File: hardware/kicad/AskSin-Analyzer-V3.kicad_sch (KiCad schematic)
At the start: 32 parts, among them J1 Pi GPIO, J2 AVR-ISP-6, J5 OLED I2C, J6 Taster, J7 WS2812, U1 MCP1754S-3302xCB, U2 ATmega328P-AU, U3 E07-900M10S, Y1 8MHz

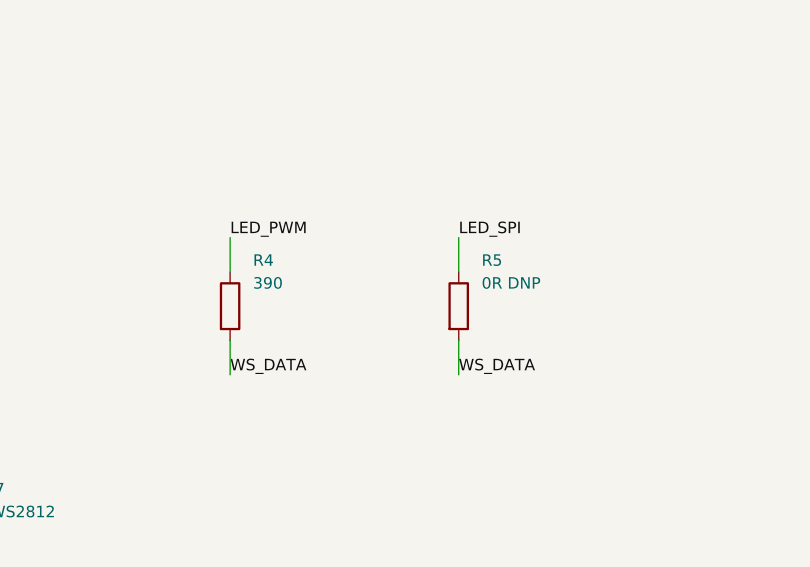
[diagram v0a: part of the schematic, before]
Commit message: Fertigungsdaten: R5 statt R4 bestückt, S1 → C231329, Y1 → C83707
Die Bestückungsvorgabe der WS2812-Datenleitung wechselt auf die
SPI-Brücke R5 (0 Ω, GPIO10, JLCPCB C17477 Basic) — den Weg nutzt die
Analyzer-Software. R4 (390 Ω, PWM/GPIO18) bleibt als dokumentierte,
unbestückte Alternative. Nur Bestückungsdaten und Werte-Texte geändert,
die Platine (Routing, Produktionsstand) ist unberührt.

Außerdem in der JLCPCB-Bestückung:
- S1 → C231329 (B3U-1000P ohne Zentrierstift; gleiche Pads, die
  Stiftbohrung bleibt leer) — C231330 war nicht lieferbar
- Y1 → C83707 (Murata CSTLS8M00G53-B0, THT-Ausnahme, Wellenlöten);
  von Hand bleiben nur noch Funkmodul und Steckverbinder

Nachgezogen: bom/cpl/jlcpcb-Dateien, Stückliste, Schaltplan-PDF
(nur Werte-Texte, ERC weiter 0/0), Fertigungs-Zip samt LIESMICH,
Reichelt-Bestellliste, Hardware-README, Status-LED-Doku, Handbuch.
generate_schematic.py überschreibt eine vorhandene .kicad_pro nicht
mehr (dort stecken die Board-Designregeln).

Co-Authored-By: Claude Fable 5 <noreply@anthropic.com>
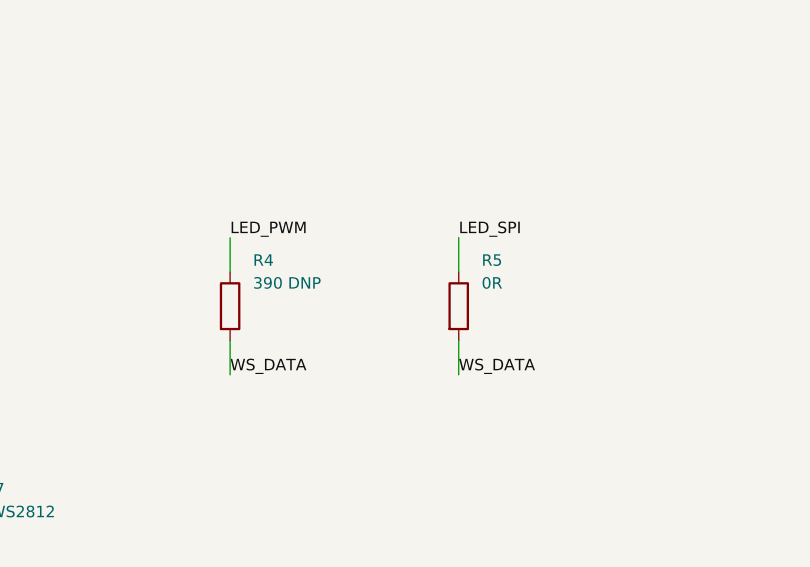
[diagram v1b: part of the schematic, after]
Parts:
- R4: value 390 -> 390 DNP
- R5: value 0R DNP -> 0R
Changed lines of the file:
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@@
 			(effects (font (size 1.27 1.27)) (justify left))
 		)
-		(property "Value" "390"
+		(property "Value" "390 DNP"
 			(at 121.92 237.49 0)
 			(effects (font (size 1.27 1.27)) (justify left))
@@
 			(effects (font (size 1.27 1.27)) (justify left))
 		)
-		(property "Value" "0R DNP"
+		(property "Value" "0R"
 			(at 147.32 237.49 0)
 			(effects (font (size 1.27 1.27)) (justify left))

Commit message: Status-LED D1 entpolt — sie konnte nie leuchten
Im KiCad-Symbol Device:LED ist Pin 1 die Kathode. Auf der Platine lag
Pin 1 an R1 (also am Treiber) und Pin 2, die Anode, an Masse. Die
Firmware schaltet ihren Pin aktiv auf HIGH (AskSinPP Led::ledOn ->
setHigh, invert() wird nie gesetzt), der Strom hätte also von Masse
gegen die Diodenrichtung zum Mikrocontroller fließen müssen.

Netzliste korrigiert: LED_TREIBER (U2.2 -> R1.1), LED_ANODE
(R1.2 -> D1.2), D1.1 an GND. Nachgerechnet: 3,9 mA bei 3,3 V und
330 Ohm mit einer roten LED — passt zu R1.

Bei der Gelegenheit ein Loch in der eigenen Prüfkette geschlossen:
rebuild.py verglich gegen die zuletzt abgelegte netlist.net statt gegen
einen frischen Export. Nach einer Schaltplanänderung prüfte es damit
gegen einen veralteten Stand — genau die Sorte stiller Fehler, die man
nicht bemerkt. Der Export läuft jetzt vor jeder Prüfung.

ERC 0/0, DRC 0/0, Netzliste exakt, alle Massepads angebunden.
Fertigungspaket und Handbuchbilder neu erzeugt.

Co-Authored-By: Claude Fable 5 <noreply@anthropic.com>
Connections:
- net GND: now also D1.1 (K); no longer D1.2 (A)
- net LED_A renamed LED_TREIBER
- net LED_K renamed LED_ANODE
- net LED_ANODE: now also D1.2 (A); no longer D1.1 (K)
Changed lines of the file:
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@@
 		(effects (font (size 1.27 1.27)) (justify left bottom))
 	)
-	(wire (pts (xy 316.23 190.5) (xy 320.04 190.5))
+	(wire (pts (xy 308.61 190.5) (xy 304.8 190.5))
 		(stroke (width 0) (type default))
 	)
 	(label "GND"
-		(at 320.04 190.5 0)
+		(at 304.8 190.5 0)
 		(fields_autoplaced yes)
 		(effects (font (size 1.27 1.27)) (justify left bottom))
@@
 		(stroke (width 0) (type default))
 	)
-	(label "LED_A"
+	(label "LED_TREIBER"
 		(at 269.24 152.4 0)
 		(fields_autoplaced yes)
@@
 		(stroke (width 0) (type default))
 	)
-	(label "LED_A"
+	(label "LED_TREIBER"
 		(at 292.1 182.88 0)
 		(fields_autoplaced yes)
@@
 		(stroke (width 0) (type default))
 	)
-	(label "LED_K"
+	(label "LED_ANODE"
 		(at 292.1 198.12 0)
 		(fields_autoplaced yes)
 		(effects (font (size 1.27 1.27)) (justify left bottom))
 	)
-	(wire (pts (xy 308.61 190.5) (xy 304.8 190.5))
-		(stroke (width 0) (type default))
-	)
-	(label "LED_K"
-		(at 304.8 190.5 0)
-		(fields_autoplaced yes)
-		(effects (font (size 1.27 1.27)) (justify left bottom))
+	(wire (pts (xy 316.23 190.5) (xy 320.04 190.5))
+		(stroke (width 0) (type default))
+	)
+	(label "LED_ANODE"
+		(at 320.04 190.5 0)
+		(fields_autoplaced yes)
+		(effects (font (size 1.27 1.27)) (justify left bottom))

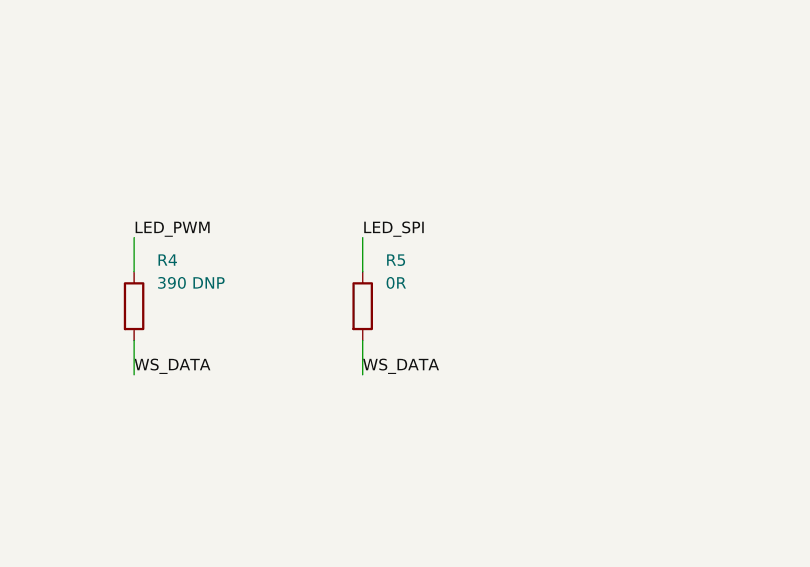
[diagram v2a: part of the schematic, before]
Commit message: R5 von 0 Ohm auf 330 Ohm — der Serienwiderstand des Vorbilds fehlte
Das Status-LED-OLED-Projekt fuehrt die WS2812-Datenleitung fuer *beide*
Ansteuerarten ueber 330-470 Ohm. Auf dem SPI-Weg war R5 bei uns eine
0-Ohm-Bruecke, der Widerstand fehlte dort also ganz. Jetzt 330 Ohm —
dasselbe Bauteil wie R1 (JLCPCB C17630), damit faellt sogar eine
Position in der Stueckliste weg (10 statt 11).

Signaltechnisch geprueft: 330 Ohm an der Eingangskapazitaet der LED
ergibt rund 5 ns Anstiegszeit gegen 420 ns kuerzeste Pulsdauer bei
2,4 MHz — unkritisch.

DRC 0/0, Netzliste exakt, alle Massepads angebunden.

Co-Authored-By: Claude Opus 5 <noreply@anthropic.com>
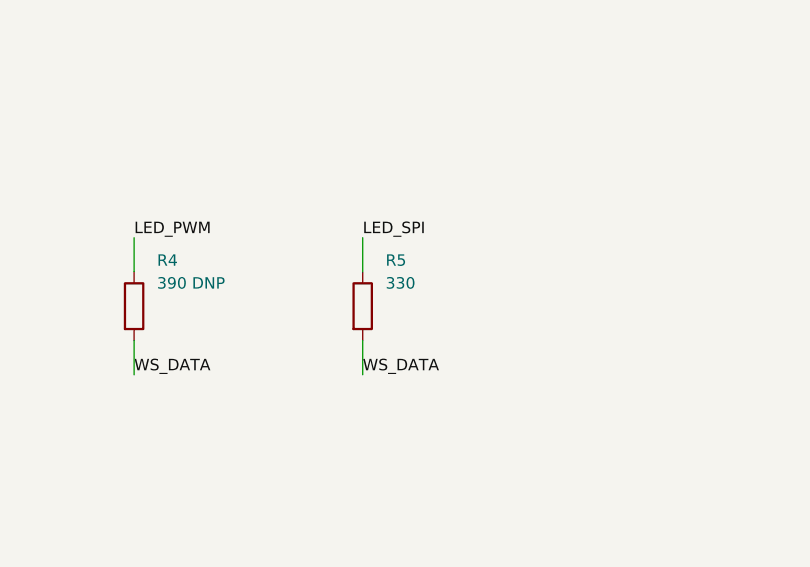
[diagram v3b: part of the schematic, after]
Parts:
- R5: value 0R -> 330
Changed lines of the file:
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@@
 			(effects (font (size 1.27 1.27)) (justify left))
 		)
-		(property "Value" "0R"
+		(property "Value" "330"
 			(at 147.32 237.49 0)
 			(effects (font (size 1.27 1.27)) (justify left))

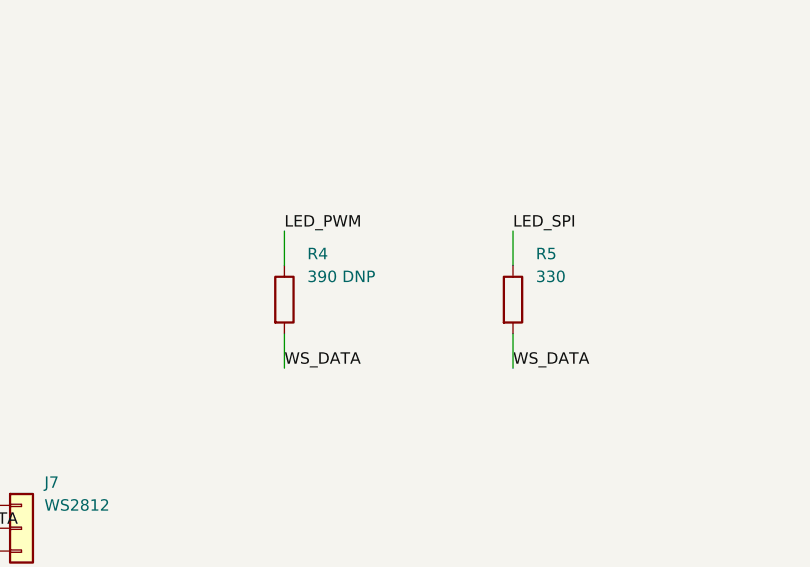
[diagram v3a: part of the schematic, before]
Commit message: Platine v0.2.0: L-Form neben dem Pi, Umschalter statt Bestueckungsvariante
Neue Bauform nach Silvios Vorgaben: Streifen hoechstens 20 mm neben dem
Pi (vorher 34), bis 80 mm lang, Schenkel an der SD-Kante entlang. Ueber
dem Pi liegt nur der 8 mm tiefe Arm fuer die 2x20-Buchse und eine
7 x 9 mm grosse Nase am hinteren Befestigungsloch — der Luefter des
PoE-HAT bleibt frei, unabhaengig vom Modell. Vier Schraubpunkte: zwei
HAT-Bohrungen im Arm, das hintere Pi-Loch in der Nase, eines im
Schenkel fuer den Tray.

Pi-Masse aus den amtlichen Zeichnungen geprueft: 85 x 56 mm, Loecher
58 x 49 mm, 3,5 mm von den Kanten — bei Pi 3B+, 4 und 5 identisch. Beim
PoE HAT (F) beginnt der Luefter rund 20 mm hinter der SD-Kante.

R4/R5 als Bestueckungsvariante entfallen. Stattdessen SPDT-Schiebe-
schalter SW1 (C&K JS102011SAQN, JLCPCB C221660) an der Aussenkante plus
EIN gemeinsamer 330-Ohm-Widerstand. Bewusst dieser Typ und nicht der
billigere MSK-12C02: fuer den JS102011SAQN gibt es einen amtlichen
KiCad-Footprint, der MSK haette von Hand gezeichnet werden muessen —
seine Landzeichnung hat ungleich verteilte Pads, das ist genau die
Sorte Fehlerquelle, die wir uns nicht leisten koennen.

Zwei eigene Fehler unterwegs gefunden und behoben: Der Innenversatz der
Kontur lief an den einspringenden Ecken in die falsche Richtung, wodurch
Freerouting Bahnen ueber die Platinenkante legte; und der Versuch, In2
als dritte Signallage freizugeben, erzeugte 120 Verstoesse inklusive
echter Kurzschluesse, weil die Stuetzvias durchgehend sind — beides
zurueckgenommen bzw. korrigiert und im Code kommentiert.

ERC 0/0, DRC 0/0, Netzliste exakt gegen die Spezifikation, alle
Massepads angebunden, J1-Pads gegen das Pi-Raster geprueft.
Fertigungspaket neu erzeugt (11 Positionen, davon 7 Basic).

Co-Authored-By: Claude Opus 5 <noreply@anthropic.com>
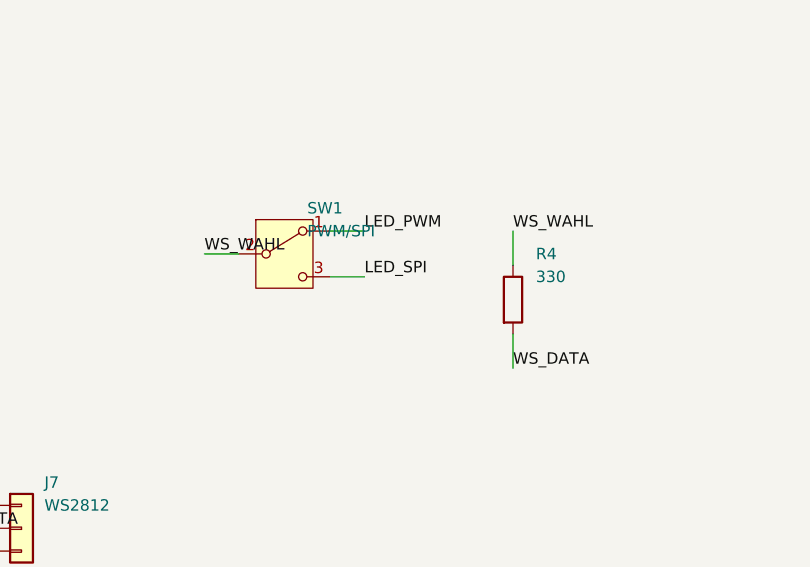
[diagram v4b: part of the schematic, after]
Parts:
- removed R5: 330, Resistor_SMD:R_0805_2012Metric_Pad1.20x1.40mm_HandSolder, symbol Device:R
- added SW1: PWM/SPI, Button_Switch_SMD:SW_SPDT_CK_JS102011SAQN, symbol Switch:SW_SPDT
- R4: value 390 DNP -> 330
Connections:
- net LED_PWM: now also SW1.1 (A); no longer R4.1
- net LED_SPI: now also SW1.3 (C)
- new net WS_WAHL: R4.1, SW1.2 (B)
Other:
- moved on the sheet: R4
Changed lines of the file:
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@@
 	)
 	(symbol
-		(lib_id "Device:R")
-		(at 119.38 240.03 0)
-		(unit 1)
-		(exclude_from_sim no)
-		(in_bom yes)
-		(on_board yes)
-		(dnp no)
-		(property "Reference" "R4"
-			(at 121.92 234.95 0)
-			(effects (font (size 1.27 1.27)) (justify left))
-		)
-		(property "Value" "390 DNP"
-			(at 121.92 237.49 0)
-			(effects (font (size 1.27 1.27)) (justify left))
-		)
-		(property "Footprint" "Resistor_SMD:R_0805_2012Metric_Pad1.20x1.40mm_HandSolder"
-			(at 119.38 240.03 0)
-			(effects (font (size 1.27 1.27)) (hide yes))
-		)
-		(property "Datasheet" "~"
-			(at 119.38 240.03 0)
-			(effects (font (size 1.27 1.27)) (hide yes))
-		)
-		(property "Description" ""
-			(at 119.38 240.03 0)
-			(effects (font (size 1.27 1.27)) (hide yes))
-		)
-		(pin "1")
-		(pin "2")
-		(instances
-			(project "AskSin-Analyzer-V3"
-				(path "/63a9f0ea-7bb9-8050-796b-649e85481845"
-					(reference "R4") (unit 1)
+		(lib_id "Switch:SW_SPDT")
+		(at 119.38 234.95 0)
+		(unit 1)
+		(exclude_from_sim no)
+		(in_bom yes)
+		(on_board yes)
+		(dnp no)
+		(property "Reference" "SW1"
+			(at 121.92 229.86999999999998 0)
+			(effects (font (size 1.27 1.27)) (justify left))
+		)
+		(property "Value" "PWM/SPI"
+			(at 121.92 232.41 0)
+			(effects (font (size 1.27 1.27)) (justify left))
+		)
+		(property "Footprint" "Button_Switch_SMD:SW_SPDT_CK_JS102011SAQN"
+			(at 119.38 234.95 0)
+			(effects (font (size 1.27 1.27)) (hide yes))
+		)
+		(property "Datasheet" "~"
+			(at 119.38 234.95 0)
+			(effects (font (size 1.27 1.27)) (hide yes))
+		)
+		(property "Description" ""
+			(at 119.38 234.95 0)
+			(effects (font (size 1.27 1.27)) (hide yes))
+		)
+		(pin "1")
+		(pin "2")
+		(pin "3")
+		(instances
+			(project "AskSin-Analyzer-V3"
+				(path "/63a9f0ea-7bb9-8050-796b-649e85481845"
+					(reference "SW1") (unit 1)
 				)
 			)
@@
 		(on_board yes)
 		(dnp no)
-		(property "Reference" "R5"
+		(property "Reference" "R4"
 			(at 147.32 234.95 0)
 			(effects (font (size 1.27 1.27)) (justify left))
@@
 			(project "AskSin-Analyzer-V3"
 				(path "/63a9f0ea-7bb9-8050-796b-649e85481845"
-					(reference "R5") (unit 1)
+					(reference "R4") (unit 1)
 				)
 			)
@@
 		(effects (font (size 1.27 1.27)) (justify left bottom))
 	)
-	(wire (pts (xy 119.38 236.22) (xy 119.38 232.41))
+	(wire (pts (xy 124.46 232.41) (xy 128.27 232.41))
 		(stroke (width 0) (type default))
 	)
 	(label "LED_PWM"
-		(at 119.38 232.41 0)
+		(at 128.27 232.41 0)
 		(fields_autoplaced yes)
 		(effects (font (size 1.27 1.27)) (justify left bottom))
@@
 		(effects (font (size 1.27 1.27)) (justify left bottom))
 	)
+	(wire (pts (xy 124.46 237.49) (xy 128.27 237.49))
+		(stroke (width 0) (type default))
+	)
+	(label "LED_SPI"
+		(at 128.27 237.49 0)
+		(fields_autoplaced yes)
+		(effects (font (size 1.27 1.27)) (justify left bottom))
+	)
+	(wire (pts (xy 114.3 234.95) (xy 110.49 234.95))
+		(stroke (width 0) (type default))
+	)
+	(label "WS_WAHL"
+		(at 110.49 234.95 0)
+		(fields_autoplaced yes)
+		(effects (font (size 1.27 1.27)) (justify left bottom))
+	)
 	(wire (pts (xy 144.78 236.22) (xy 144.78 232.41))
 		(stroke (width 0) (type default))
 	)
-	(label "LED_SPI"
+	(label "WS_WAHL"
 		(at 144.78 232.41 0)
 		(fields_autoplaced yes)
 		(effects (font (size 1.27 1.27)) (justify left bottom))
-	)
-	(wire (pts (xy 119.38 243.84) (xy 119.38 247.65))
-		(stroke (width 0) (type default))
-	)
-	(label "WS_DATA"
-		(at 119.38 247.65 0)
-		(fields_autoplaced yes)
-		(effects (font (size 1.27 1.27)) (justify left bottom))
